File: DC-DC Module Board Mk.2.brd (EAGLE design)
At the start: 177.9 x 101.7 mm, 151 parts, among them T1 FDN340P, T2 AP1117_LIN_REG, U3 LM1085IS-5.0

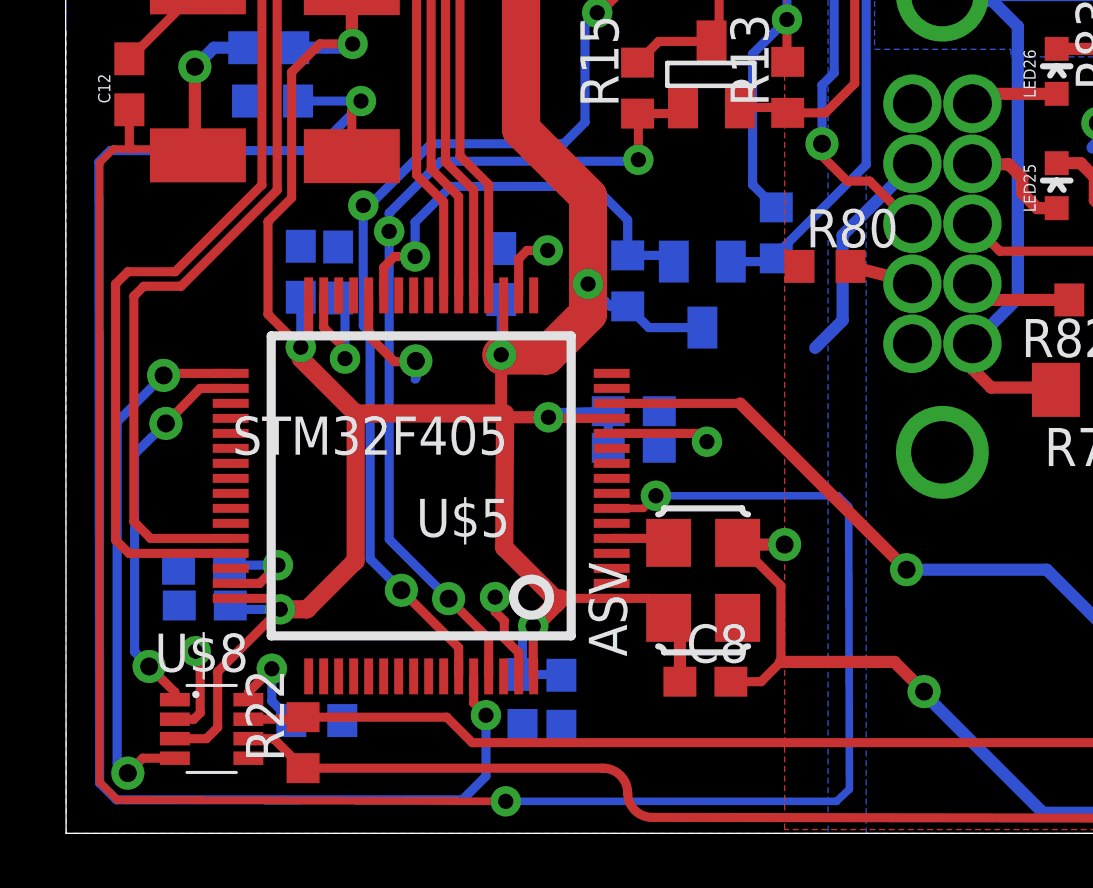
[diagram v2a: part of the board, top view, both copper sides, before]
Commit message: Replaced the stm32f405 chip with a corrected version
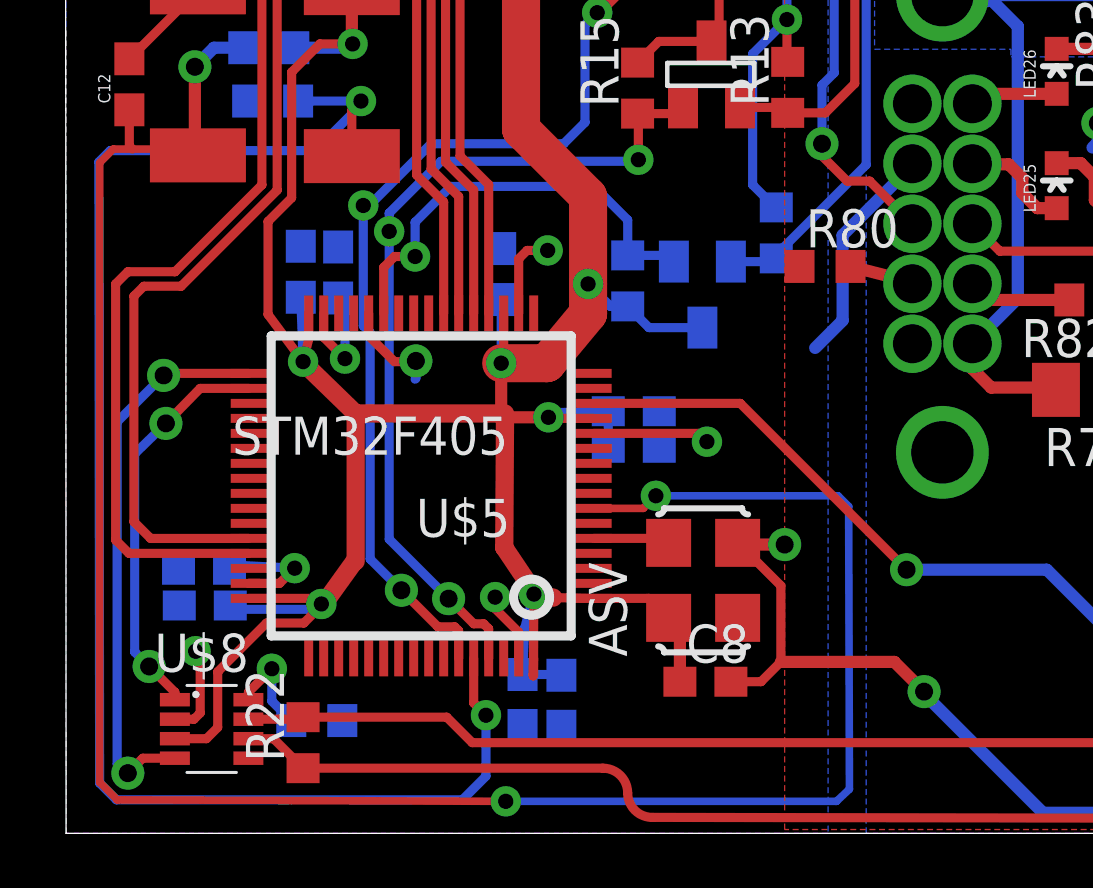
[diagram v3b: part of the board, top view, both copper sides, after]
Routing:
- net +3V3: track 139.6 -> 142.9 mm
- net VCAP_2: track 3.50 -> 4.35 mm
- net TXD: track 12.9 -> 13.5 mm
- net RXD: track 18.1 -> 18.7 mm
- net PWM_IN: track 14.4 -> 15.0 mm
- net PIN23: track 27.7 -> 28.3 mm
- net PIN22: track 29.5 -> 30.1 mm
- net PIN21: track 30.9 -> 31.5 mm
- net USBD+: track 32.0 -> 32.6 mm
- net OSCIN: track 1.96 -> 2.56 mm
- net PIN20: track 32.4 -> 33.0 mm
- net NRST: track 73.6 -> 74.2 mm
- net BOOT0: track 51.9 -> 52.5 mm
- net PA0_PWM: track 388.4 -> 389.0 mm
- net USBD-: track 32.4 -> 33.0 mm

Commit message: drc error fixes
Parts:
- moved LED14 10.5 mm to (32.7, 69.7), turned to 90 degrees
- moved R43 10.2 mm to (32.1, 71.8), turned to 180 degrees
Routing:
- net DGND: track 463.4 -> 499.1 mm
- net GND: track 105.1 -> 93.4 mm
- net +12V2: track 29.3 -> 21.7 mm, vias 2 -> 0
- net +5V: track 99.7 -> 98.4 mm

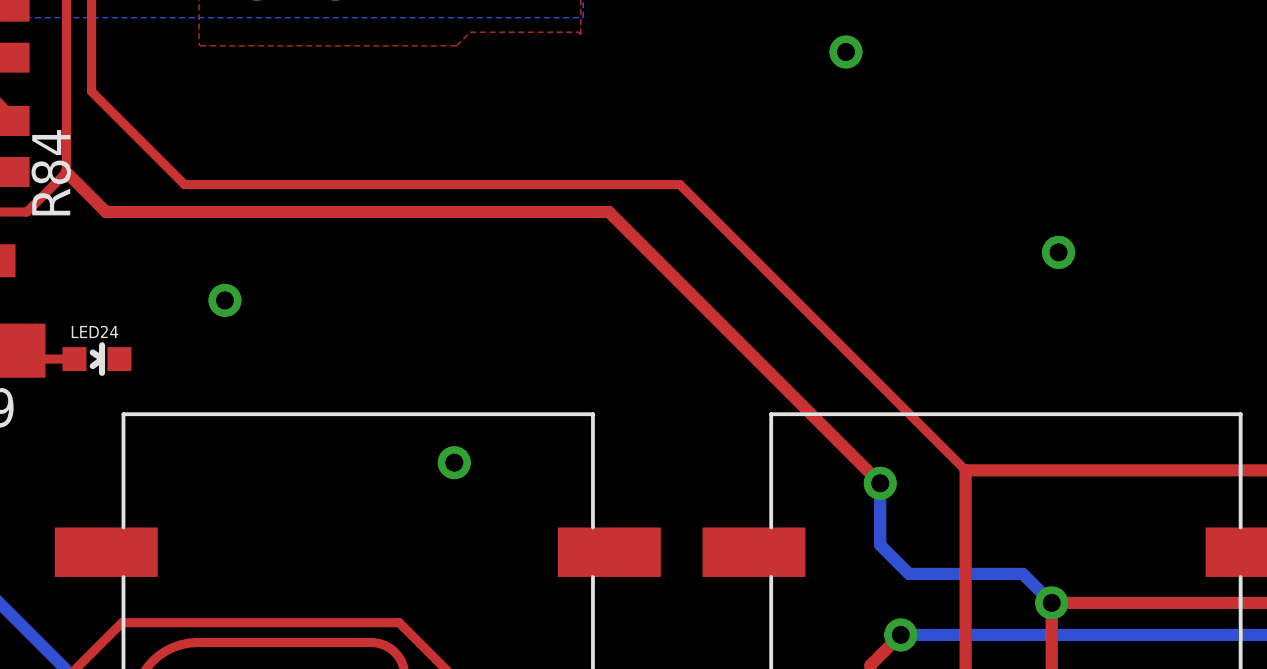
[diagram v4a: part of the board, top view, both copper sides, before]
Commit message: SCL and SDA test vias
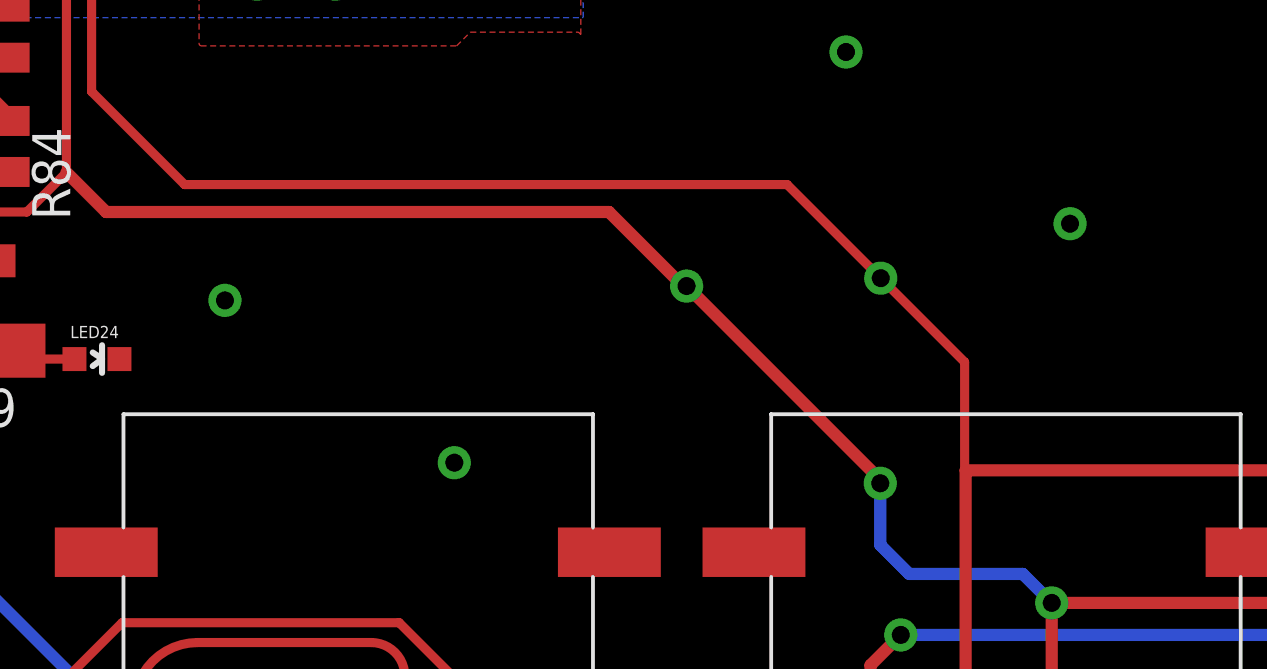
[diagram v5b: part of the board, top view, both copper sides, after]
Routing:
- net SDA: track 502.5 -> 504.6 mm, vias 11 -> 12
- net SCL: vias 14 -> 15
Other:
- board text added: "SCL test"
- board text added: "SDA test"
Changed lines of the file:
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@@
 <layer number="25" name="tNames" color="7" fill="1" visible="yes" active="yes"/>
 <layer number="26" name="bNames" color="7" fill="1" visible="yes" active="yes"/>
-<layer number="27" name="tValues" color="7" fill="1" visible="no" active="yes"/>
+<layer number="27" name="tValues" color="7" fill="1" visible="yes" active="yes"/>
 <layer number="28" name="bValues" color="7" fill="1" visible="no" active="yes"/>
 <layer number="29" name="tStop" color="7" fill="3" visible="no" active="yes"/>
@@
 <text x="2.8702" y="28.1178" size="0.8128" layer="21">RESET</text>
 <text x="7.8486" y="28.067" size="0.8128" layer="21">BOOT</text>
+<text x="50.116" y="14.817" size="1.016" layer="27">SCL test</text>
+<text x="65.879" y="15.677" size="1.016" layer="27">SDA test</text>
 </plain>
 <attributes>
@@
 <via x="47.5742" y="37.211" extent="1-16" drill="0.6"/>
 <via x="63.3222" y="23.4696" extent="1-16" drill="0.6"/>
-<via x="70.4088" y="16.7894" extent="1-16" drill="0.6"/>
+<via x="70.7908" y="17.7444" extent="1-16" drill="0.6"/>
 <via x="42.6212" y="15.1892" extent="1-16" drill="0.6"/>
 <via x="50.2666" y="9.779" extent="1-16" drill="0.6"/>
@@
 <wire x1="64.4652" y1="7.0358" x2="64.4652" y2="9.0932" width="0.4064" layer="16"/>
 <via x="64.4652" y="9.0932" extent="1-16" drill="0.6"/>
-<wire x1="64.4652" y1="9.0932" x2="55.4228" y2="18.1356" width="0.4064" layer="1"/>
 <wire x1="37.338" y1="26.924" x2="36.7284" y2="27.5336" width="0.3048" layer="1"/>
 <wire x1="36.7284" y1="27.5336" x2="33.3756" y2="27.5336" width="0.3048" layer="1"/>
@@
 <wire x1="129.883" y1="63.594" x2="129.883" y2="61.068" width="0.4064" layer="1"/>
 <wire x1="129.883" y1="61.068" x2="129.83" y2="61.015" width="0.4064" layer="1"/>
+<wire x1="64.4652" y1="9.0932" x2="64.4652" y2="9.2108" width="0.4064" layer="1"/>
+<wire x1="64.4652" y1="9.2108" x2="58.009" y2="15.667" width="0.4064" layer="1"/>
+<via x="58.009" y="15.667" extent="1-16" drill="0.6"/>
+<wire x1="58.009" y1="15.667" x2="57.8914" y2="15.667" width="0.4064" layer="1"/>
+<wire x1="57.8914" y1="15.667" x2="55.4228" y2="18.1356" width="0.4064" layer="1"/>
 </signal>
 <signal name="SDA">
@@
 <wire x1="81.026" y1="65.024" x2="62.6618" y2="65.0494" width="0.4064" layer="16"/>
 <wire x1="27.9908" y1="31.2928" x2="29.1592" y2="31.2928" width="0.3048" layer="1"/>
-<wire x1="41.275" y1="19.05" x2="57.785" y2="19.05" width="0.3048" layer="1"/>
-<wire x1="57.785" y1="19.05" x2="67.31" y2="9.525" width="0.3048" layer="1"/>
+<wire x1="41.275" y1="19.05" x2="61.361" y2="19.05" width="0.3048" layer="1"/>
 <wire x1="67.31" y1="9.525" x2="83.058" y2="9.525" width="0.4064" layer="1"/>
 <wire x1="83.058" y1="9.525" x2="83.82" y2="10.287" width="0.4064" layer="1"/>
@@
 <wire x1="163.83" y1="10.16" x2="167.64" y2="10.16" width="0.3048" layer="16"/>
 <wire x1="169.08" y1="8.72" x2="167.64" y2="10.16" width="0.4064" layer="1"/>
+<wire x1="61.361" y1="19.05" x2="64.481" y2="15.93" width="0.3048" layer="1"/>
+<via x="64.481" y="15.93" extent="1-16" drill="0.6"/>
+<wire x1="67.31" y1="9.525" x2="67.277" y2="9.525" width="0.3048" layer="1"/>
+<wire x1="67.277" y1="9.525" x2="67.277" y2="13.134" width="0.3048" layer="1"/>
+<wire x1="67.277" y1="13.134" x2="64.481" y2="15.93" width="0.3048" layer="1"/>
 </signal>
 <signal name="ALERT">

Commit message: many aesthetic corrections
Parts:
- C14, C15, C16: value .1u -> .1uF
- C19, C20: value 15u -> 15uF
- C21: value 10u -> 10uF
- renumbered T1 to Q1, T2 to U2, U$7 to J$7
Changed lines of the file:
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@@
 <attribute name="BOM" value="INCLUDE" x="95.25" y="80.01" size="1.778" layer="27" rot="R90" display="off"/>
 </element>
-<element name="C19" library="rcl" package="C3216" value="15u" x="87.63" y="91.44" rot="R90"/>
-<element name="C20" library="rcl" package="C3216" value="15u" x="90.17" y="91.44" rot="R90"/>
-<element name="C21" library="rcl" package="C0603" value="10u" x="85.09" y="90.805" rot="R90"/>
-<element name="C14" library="rcl" package="C0603" value=".1u" x="133.35" y="92.71" rot="R270"/>
-<element name="C15" library="rcl" package="C0603" value=".1u" x="130.81" y="92.71" rot="R270"/>
-<element name="C16" library="rcl" package="C0603" value=".1u" x="127" y="92.71" rot="R270"/>
+<element name="C19" library="rcl" package="C3216" value="15uF" x="87.63" y="91.44" rot="R90"/>
+<element name="C20" library="rcl" package="C3216" value="15uF" x="90.17" y="91.44" rot="R90"/>
+<element name="C21" library="rcl" package="C0603" value="10uF" x="85.09" y="90.805" rot="R90"/>
+<element name="C14" library="rcl" package="C0603" value=".1uF" x="133.35" y="92.71" rot="R270"/>
+<element name="C15" library="rcl" package="C0603" value=".1uF" x="130.81" y="92.71" rot="R270"/>
+<element name="C16" library="rcl" package="C0603" value=".1uF" x="127" y="92.71" rot="R270"/>
 <element name="U$2" library="Connectors" package="XT60" value="XT60" x="95.25" y="54.61" rot="R90"/>
 <element name="C22" library="ux-capacitor" package="NICHICON-UX-8X10" value="10uF" x="120.65" y="91.44"/>
@@
 <attribute name="BOM" value="INCLUDE" x="140.97" y="2.54" size="1.778" layer="27" rot="R90" display="off"/>
 </element>
-<element name="U$7" library="Other" package="MICRO_B" value="MICROUSB" x="0" y="33.02" rot="R270"/>
+<element name="J$7" library="Other" package="MICRO_B" value="MICROUSB" x="0" y="33.02" rot="R270"/>
 <element name="RN1" library="DiscreteComponents" package="EXBV4V" value="" x="7.2136" y="33.3248" rot="R270">
 <attribute name="MPN" value="MNR12ERAPJ220" x="22.4536" y="42.2148" size="1.778" layer="27" rot="R270" display="off"/>
@@
 <attribute name="DIGIKEY" value="RHM1381CT-ND" x="22.4536" y="42.2148" size="1.778" layer="27" rot="R270" display="off"/>
 </element>
-<element name="T1" library="DiscreteComponents" package="SOT-23" value="FDN340P" x="8.9154" y="36.1442" rot="R270">
+<element name="Q1" library="DiscreteComponents" package="SOT-23" value="FDN340P" x="8.9154" y="36.1442" rot="R270">
 <attribute name="DIGIKEY" value="FDN340PCT-ND" x="6.3754" y="36.1442" size="1.778" layer="27" rot="R270" display="off"/>
 </element>
 <element name="D2" library="DiscreteComponents" package="DO-214AC" value="" x="12.4714" y="36.0934" rot="R270"/>
-<element name="T2" library="PowerComponents" package="SOT223" value="AP1117_LIN_REG" x="17.653" y="34.9758" rot="R180"/>
+<element name="U2" library="PowerComponents" package="SOT223" value="AP1117_LIN_REG" x="17.653" y="34.9758" rot="R180"/>
 <element name="C1" library="rcl" package="C0603" value="0.22uF" x="14.5034" y="40.1066" rot="R180"/>
 <element name="C25" library="rcl" package="C0603" value="0.22uF" x="18.669" y="40.1574"/>
@@
 <contactref element="C25" pad="2"/>
 <contactref element="C1" pad="2"/>
-<contactref element="T2" pad="GND"/>
-<contactref element="U$7" pad="P5"/>
-<contactref element="U$7" pad="GND3"/>
-<contactref element="U$7" pad="GND1"/>
-<contactref element="U$7" pad="GND4"/>
-<contactref element="U$7" pad="GND7"/>
-<contactref element="U$7" pad="GND2"/>
-<contactref element="U$7" pad="GND8"/>
-<contactref element="U$7" pad="P4"/>
+<contactref element="U2" pad="GND"/>
+<contactref element="J$7" pad="P5"/>
+<contactref element="J$7" pad="GND3"/>
+<contactref element="J$7" pad="GND1"/>
+<contactref element="J$7" pad="GND4"/>
+<contactref element="J$7" pad="GND7"/>
+<contactref element="J$7" pad="GND2"/>
+<contactref element="J$7" pad="GND8"/>
+<contactref element="J$7" pad="P4"/>
 <contactref element="U$8" pad="2"/>
 <contactref element="R17" pad="1"/>
@@
 <contactref element="U$8" pad="3"/>
 <contactref element="C25" pad="1"/>
-<contactref element="T2" pad="VOUT"/>
-<contactref element="T2" pad="TAB"/>
+<contactref element="U2" pad="VOUT"/>
+<contactref element="U2" pad="TAB"/>
 <contactref element="R21" pad="2"/>
 <contactref element="R30" pad="2"/>
@@
 <contactref element="D10" pad="1"/>
 <contactref element="C29" pad="2"/>
-<contactref element="T1" pad="3"/>
+<contactref element="Q1" pad="3"/>
 <contactref element="D2" pad="A"/>
 <contactref element="U$30" pad="C2"/>
@@
 </signal>
 <signal name="N$24">
-<contactref element="U$7" pad="P3"/>
+<contactref element="J$7" pad="P3"/>
 <contactref element="RN1" pad="2"/>
 <wire x1="4.15" y1="33.02" x2="6.4386" y2="33.02" width="0.3048" layer="1"/>
@@
 </signal>
 <signal name="N$57">
-<contactref element="U$7" pad="P1"/>
-<contactref element="T1" pad="1"/>
+<contactref element="J$7" pad="P1"/>
+<contactref element="Q1" pad="1"/>
 <wire x1="4.15" y1="34.32" x2="5.0338" y2="34.32" width="0.4064" layer="1"/>
 <wire x1="5.0338" y1="34.32" x2="6.8072" y2="36.0934" width="0.4064" layer="1"/>
@@
 <signal name="N$58">
 <contactref element="D2" pad="C"/>
-<contactref element="T1" pad="2"/>
-<contactref element="T2" pad="VIN"/>
+<contactref element="Q1" pad="2"/>
+<contactref element="U2" pad="VIN"/>
 <contactref element="C1" pad="1"/>
 <wire x1="12.4714" y1="38.1184" x2="10.9658" y2="38.1184" width="0.4064" layer="1"/>
@@
 <signal name="N$9">
 <contactref element="RN1" pad="1"/>
-<contactref element="U$7" pad="P2"/>
+<contactref element="J$7" pad="P2"/>
 <wire x1="4.15" y1="33.67" x2="6.4386" y2="33.67" width="0.3048" layer="1"/>
 <wire x1="6.4386" y1="33.67" x2="6.4386" y2="33.7248" width="0.3048" layer="1"/>
